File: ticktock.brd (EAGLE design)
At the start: 61 x 67.3 mm, 63 parts, among them IC1 ATMEGA644A, IC2 AD8611RM, IC3 REF200U, J1 AVR_SPI_PRG_6NS, Q1 MOSFET-NCHANNEL2N7002PW, Q2 MOSFET-NCHANNELBSS138, Q3 MOSFET-NCHANNELBSS138, U1 MAX232SOIC16, U2 OSCILLATORSMD, U3 FT232RLSSOP, U4 BMP180, X1 RS232

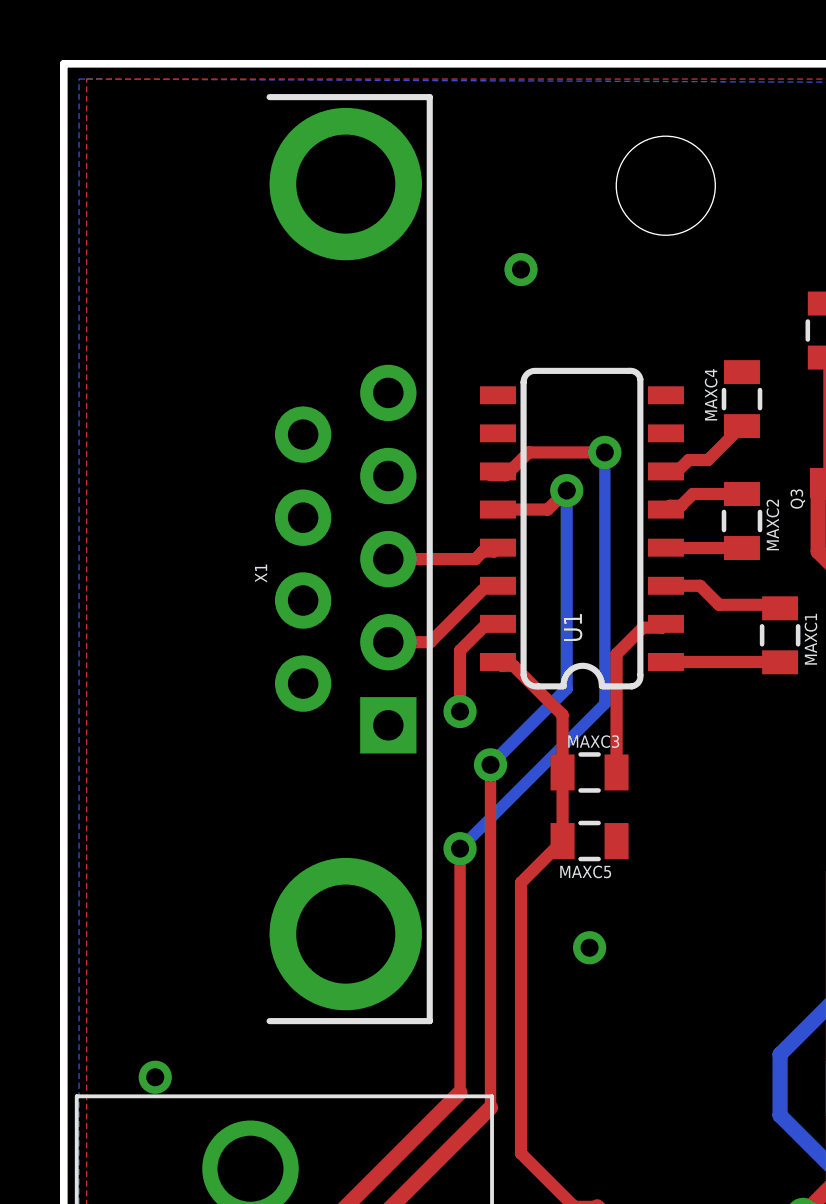
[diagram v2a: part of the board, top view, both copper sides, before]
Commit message: Replace DB9 female connector with a male one
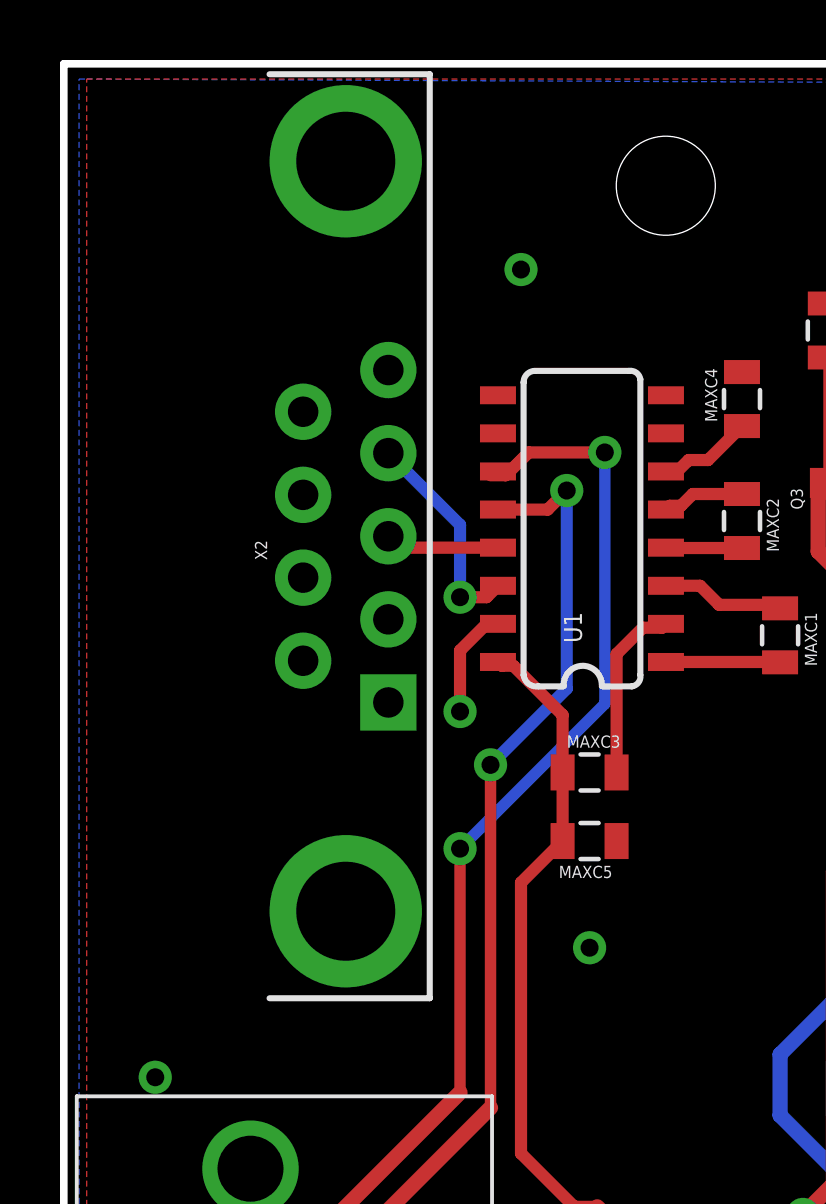
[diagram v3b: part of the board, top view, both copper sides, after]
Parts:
- removed X1: RS232, SparkFun-Connectors:DB9
- added X2: (no value), SparkFun-Connectors:DB9_MALE
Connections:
- net GND: now also X2.5; no longer X1.5
- net N$10: now also X2.3; no longer X1.3
- net N$8: now also X2.2; no longer X1.2
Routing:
- net N$8: track 3.88 -> 7.21 mm, vias 0 -> 1
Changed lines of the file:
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@@
 <element name="MAXC5" library="SparkFun-Capacitors" package="0805" value="1uF" x="17.526" y="41.402" rot="R180"/>
 <element name="MAXC4" library="SparkFun-Capacitors" package="0805" value="1uF" x="22.606" y="56.134" rot="R90"/>
-<element name="X1" library="SparkFun-Connectors" package="DB9" value="RS232" x="9.398" y="50.8" rot="R90"/>
 <element name="GPS_10MHZ_IN" library="SparkFun-Connectors" package="BNC" value="BNCPTH" x="11.303" y="25.4" rot="R90"/>
 <element name="GPS_1PPS_IN" library="SparkFun-Connectors" package="BNC" value="BNCPTH" x="11.303" y="8.128" rot="R90"/>
-<element name="IC1" library="atmel" package="TQFP44" value="ATMEGA644A" x="38.1" y="22.86"/>
+<element name="IC1" library="atmel" package="TQFP44" value="ATMEGA644A" x="38.1" y="22.86">
+<attribute name="OC_NEWARK" value="58M3748" x="38.1" y="22.86" size="1.778" layer="27" display="off"/>
+<attribute name="MPN" value="ATMEGA644PV-10AU" x="38.1" y="22.86" size="1.778" layer="27" display="off"/>
+<attribute name="MF" value="" x="38.1" y="22.86" size="1.778" layer="27" display="off"/>
+<attribute name="OC_FARNELL" value="1455123" x="38.1" y="22.86" size="1.778" layer="27" display="off"/>
+</element>
 <element name="U3" library="SparkFun-DigitalIC" package="SSOP28DB" value="FT232RLSSOP" x="30.48" y="5.08" rot="R180">
 <attribute name="PROD_ID" value="IC-00870" x="30.48" y="5.08" size="1.778" layer="27" rot="R180" display="off"/>
@@
 <element name="U$1" library="tickTockLibrary" package="MSOP08" value="OPA381" x="56.134" y="20.32" rot="R270"/>
 <element name="U4" library="SparkFun-Sensors" package="BMP180" value="BMP180" x="31.75" y="59.69" rot="R90"/>
-<element name="IC3" library="burr-brown" package="SO08" value="REF200U" x="49.53" y="35.56" rot="R270"/>
+<element name="IC3" library="burr-brown" package="SO08" value="REF200U" x="49.53" y="35.56" rot="R270">
+<attribute name="OC_NEWARK" value="34C7615" x="49.53" y="35.56" size="1.778" layer="27" rot="R270" display="off"/>
+<attribute name="MPN" value="REF200AU" x="49.53" y="35.56" size="1.778" layer="27" rot="R270" display="off"/>
+<attribute name="MF" value="TEXAS INSTRUMENTS" x="49.53" y="35.56" size="1.778" layer="27" rot="R270" display="off"/>
+<attribute name="OC_FARNELL" value="1207240" x="49.53" y="35.56" size="1.778" layer="27" rot="R270" display="off"/>
+</element>
 <element name="SJ1" library="SparkFun" package="SJ_2S-NO" value="SOLDERJUMPERNO" x="57.15" y="34.29" rot="R180"/>
 <element name="SJ2" library="SparkFun" package="SJ_2S-NO" value="SOLDERJUMPERNO" x="57.15" y="38.1" rot="R90"/>
@@
 <element name="STANDOFF4" library="SparkFun-Electromechanical" package="STAND-OFF" value="STAND-OFF" x="17.018" y="3.556"/>
 <element name="JP9" library="SparkFun-Connectors" package="1X03_LOCK" value="3-Pin" x="16.51" y="10.16" rot="R90"/>
+<element name="X2" library="SparkFun-Connectors" package="DB9_MALE" value="" x="9.398" y="51.562" rot="R90"/>
 </elements>
 <signals>
@@
 <contactref element="MAXC5" pad="1"/>
 <contactref element="MAXC4" pad="2"/>
-<contactref element="X1" pad="5"/>
 <contactref element="IC1" pad="18"/>
 <contactref element="IC1" pad="6"/>
@@
 <wire x1="14.097" y1="48.641" x2="13.208" y2="47.752" width="0.4064" layer="1"/>
 <wire x1="13.208" y1="47.752" x2="13.208" y2="45.72" width="0.4064" layer="1"/>
+<contactref element="X2" pad="5"/>
 <wire x1="28.205" y1="1.424" x2="30.155" y2="1.424" width="0" layer="19" extent="1-1"/>
 </signal>
@@
 <signal name="N$8">
 <contactref element="U1" pad="14"/>
-<contactref element="X1" pad="2"/>
-<wire x1="10.818" y1="48.03" x2="12.216" y2="48.03" width="0.4064" layer="1"/>
-<wire x1="12.216" y1="48.03" x2="13.97" y2="49.784" width="0.4064" layer="1"/>
-<wire x1="13.97" y1="49.784" x2="14.472" y2="49.911" width="0" layer="19" extent="1-1"/>
+<contactref element="X2" pad="2"/>
+<wire x1="14.472" y1="49.911" x2="14.091" y2="49.53" width="0.4064" layer="1"/>
+<wire x1="14.091" y1="49.53" x2="13.208" y2="49.53" width="0.4064" layer="1"/>
+<via x="13.208" y="49.53" extent="1-16" drill="0.6"/>
+<wire x1="10.818" y1="54.332" x2="13.208" y2="51.942" width="0.4064" layer="16"/>
+<wire x1="13.208" y1="51.942" x2="13.208" y2="49.53" width="0.4064" layer="16"/>
 </signal>
 <signal name="N$10">
 <contactref element="U1" pad="13"/>
-<contactref element="X1" pad="3"/>
-<wire x1="10.818" y1="50.8" x2="13.716" y2="50.8" width="0.4064" layer="1"/>
-<wire x1="13.716" y1="50.8" x2="13.97" y2="51.054" width="0.4064" layer="1"/>
-<wire x1="13.97" y1="51.054" x2="14.345" y2="51.054" width="0.4064" layer="1"/>
-<wire x1="14.345" y1="51.054" x2="14.472" y2="51.181" width="0.4064" layer="1"/>
+<contactref element="X2" pad="3"/>
+<wire x1="14.472" y1="51.181" x2="11.199" y2="51.181" width="0.4064" layer="1"/>
+<wire x1="11.199" y1="51.181" x2="10.818" y2="51.562" width="0.4064" layer="1"/>
 </signal>
 <signal name="GPS_1PPS">

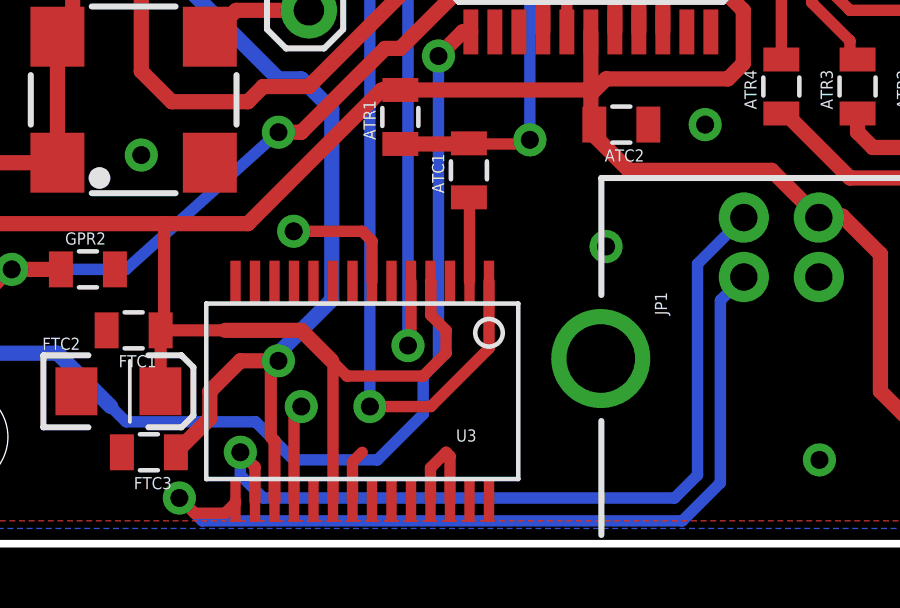
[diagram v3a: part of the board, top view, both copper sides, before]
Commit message: Flip USB_TX and USB_RX in schematic
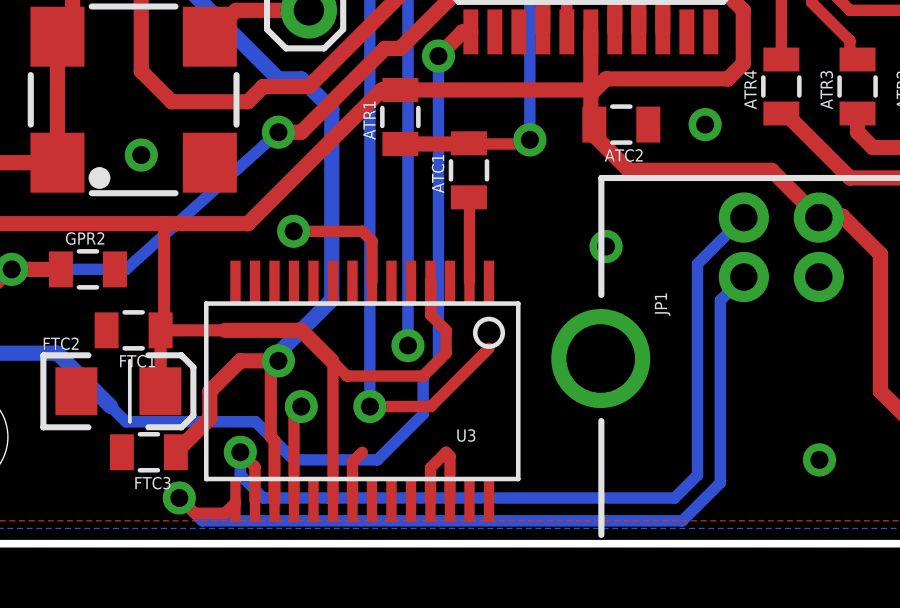
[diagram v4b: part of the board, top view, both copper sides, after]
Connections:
- net USB_RX: now also IC1.10; no longer IC1.9
- net USB_TX: now also IC1.9; no longer IC1.10
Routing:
- net USB_TX: track 24.0 -> 17.8 mm
- net USB_RX: track 19.8 -> 21.8 mm
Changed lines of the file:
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@@
 <wire x1="42.418" y1="8.108" x2="43.2" y2="8.89" width="0.381" layer="16"/>
 </signal>
-<signal name="USB_TX">
-<contactref element="U3" pad="1"/>
+<signal name="USB_RX">
 <contactref element="IC1" pad="10"/>
-<wire x1="34.705" y1="8.736" x2="34.705" y2="6.511" width="0.381" layer="1"/>
 <wire x1="34.705" y1="6.511" x2="32.766" y2="4.572" width="0.381" layer="1"/>
 <via x="30.734" y="4.572" extent="1-16" drill="0.6"/>
@@
 <wire x1="30.836" y1="19.66" x2="32.3" y2="19.66" width="0.381" layer="1"/>
 <wire x1="32.766" y1="4.572" x2="30.734" y2="4.572" width="0.381" layer="1"/>
+<contactref element="U3" pad="5"/>
+<wire x1="34.705" y1="6.511" x2="32.105" y2="8.736" width="0" layer="19" extent="1-1"/>
 </signal>
-<signal name="USB_RX">
-<contactref element="U3" pad="5"/>
+<signal name="USB_TX">
 <contactref element="IC1" pad="9"/>
-<wire x1="32.105" y1="8.736" x2="32.105" y2="6.705" width="0.381" layer="1"/>
 <wire x1="32.105" y1="6.705" x2="32.004" y2="6.604" width="0.381" layer="1"/>
 <via x="32.004" y="6.604" extent="1-16" drill="0.6"/>
@@
 <wire x1="34.544" y1="20.828" x2="34.176" y2="20.46" width="0.381" layer="1"/>
 <wire x1="34.176" y1="20.46" x2="32.3" y2="20.46" width="0.381" layer="1"/>
+<contactref element="U3" pad="1"/>
+<wire x1="32.105" y1="6.705" x2="34.705" y2="8.736" width="0" layer="19" extent="1-1"/>
 </signal>
 <signal name="3.3V">

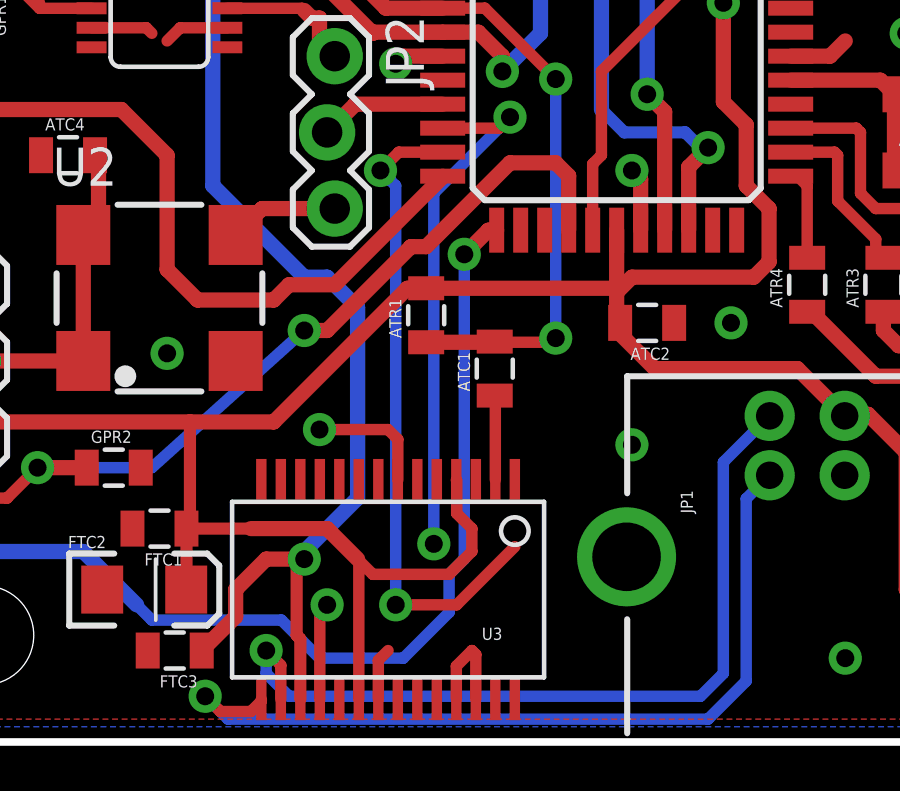
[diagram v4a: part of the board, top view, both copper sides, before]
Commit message: Flip USB_TX and USB_RX in board
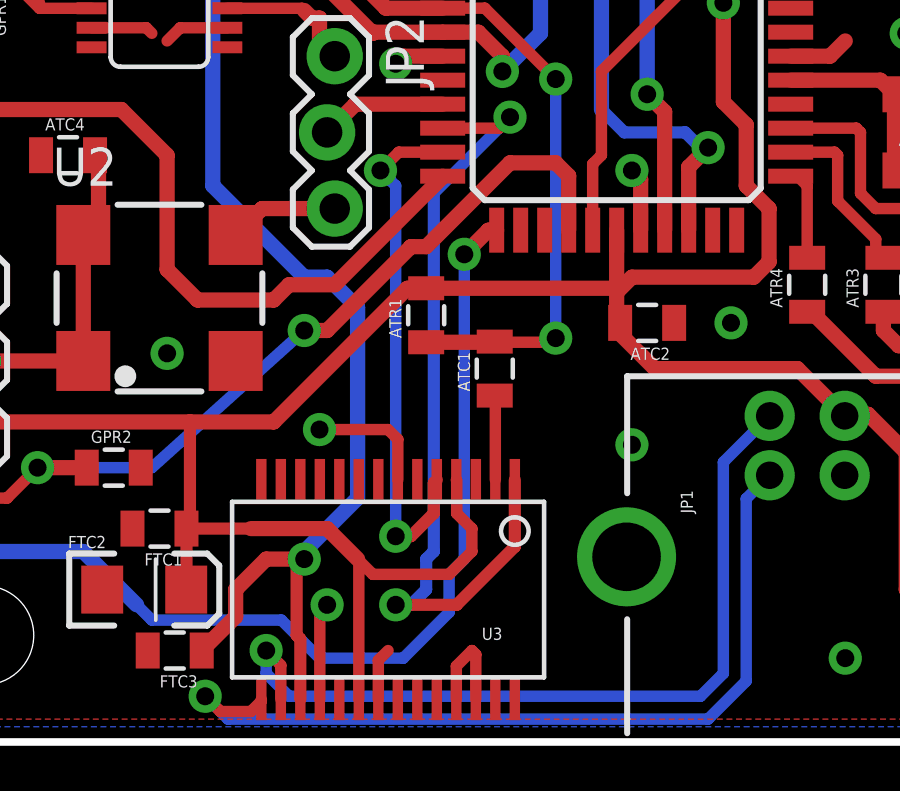
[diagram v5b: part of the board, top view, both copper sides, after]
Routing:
- net USB_TX: track 17.8 -> 27.5 mm
- net USB_RX: track 21.8 -> 17.5 mm
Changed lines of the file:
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@@
 <signal name="USB_RX">
 <contactref element="IC1" pad="10"/>
-<wire x1="34.705" y1="6.511" x2="32.766" y2="4.572" width="0.381" layer="1"/>
-<via x="30.734" y="4.572" extent="1-16" drill="0.6"/>
-<wire x1="30.734" y1="4.572" x2="30.734" y2="18.542" width="0.381" layer="16"/>
+<via x="30.734" y="6.858" extent="1-16" drill="0.6"/>
+<wire x1="30.734" y1="6.858" x2="30.734" y2="18.542" width="0.381" layer="16"/>
 <wire x1="30.734" y1="18.542" x2="30.226" y2="19.05" width="0.381" layer="16"/>
 <via x="30.226" y="19.05" extent="1-16" drill="0.6"/>
 <wire x1="30.226" y1="19.05" x2="30.836" y2="19.66" width="0.381" layer="1"/>
 <wire x1="30.836" y1="19.66" x2="32.3" y2="19.66" width="0.381" layer="1"/>
-<wire x1="32.766" y1="4.572" x2="30.734" y2="4.572" width="0.381" layer="1"/>
 <contactref element="U3" pad="5"/>
-<wire x1="34.705" y1="6.511" x2="32.105" y2="8.736" width="0" layer="19" extent="1-1"/>
+<wire x1="32.105" y1="8.736" x2="32.004" y2="8.635" width="0.4064" layer="1"/>
+<wire x1="32.004" y1="8.635" x2="32.004" y2="7.62" width="0.4064" layer="1"/>
+<wire x1="32.004" y1="7.62" x2="31.242" y2="6.858" width="0.4064" layer="1"/>
+<wire x1="31.242" y1="6.858" x2="30.734" y2="6.858" width="0.4064" layer="1"/>
 </signal>
 <signal name="USB_TX">
 <contactref element="IC1" pad="9"/>
-<wire x1="32.105" y1="6.705" x2="32.004" y2="6.604" width="0.381" layer="1"/>
-<via x="32.004" y="6.604" extent="1-16" drill="0.6"/>
-<wire x1="32.004" y1="6.604" x2="32.004" y2="18.288" width="0.381" layer="16"/>
+<via x="30.734" y="4.572" extent="1-16" drill="0.6"/>
 <wire x1="32.004" y1="18.288" x2="34.544" y2="20.828" width="0.381" layer="16"/>
 <via x="34.544" y="20.828" extent="1-16" drill="0.6"/>
@@
 <wire x1="34.176" y1="20.46" x2="32.3" y2="20.46" width="0.381" layer="1"/>
 <contactref element="U3" pad="1"/>
-<wire x1="32.105" y1="6.705" x2="34.705" y2="8.736" width="0" layer="19" extent="1-1"/>
+<wire x1="31.75" y1="6.096" x2="32.004" y2="6.35" width="0.4064" layer="16"/>
+<wire x1="32.004" y1="6.35" x2="32.004" y2="18.288" width="0.4064" layer="16"/>
+<wire x1="31.75" y1="6.096" x2="31.75" y2="5.08" width="0.4064" layer="16"/>
+<wire x1="31.75" y1="5.08" x2="31.242" y2="4.572" width="0.4064" layer="16"/>
+<wire x1="31.242" y1="4.572" x2="30.734" y2="4.572" width="0.4064" layer="16"/>
+<wire x1="30.734" y1="4.572" x2="32.766" y2="4.572" width="0.4064" layer="1"/>
+<wire x1="32.766" y1="4.572" x2="34.705" y2="6.511" width="0.4064" layer="1"/>
+<wire x1="34.705" y1="6.511" x2="34.705" y2="8.736" width="0.4064" layer="1"/>
 </signal>
 <signal name="3.3V">
